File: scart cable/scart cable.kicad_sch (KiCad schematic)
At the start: 12 parts

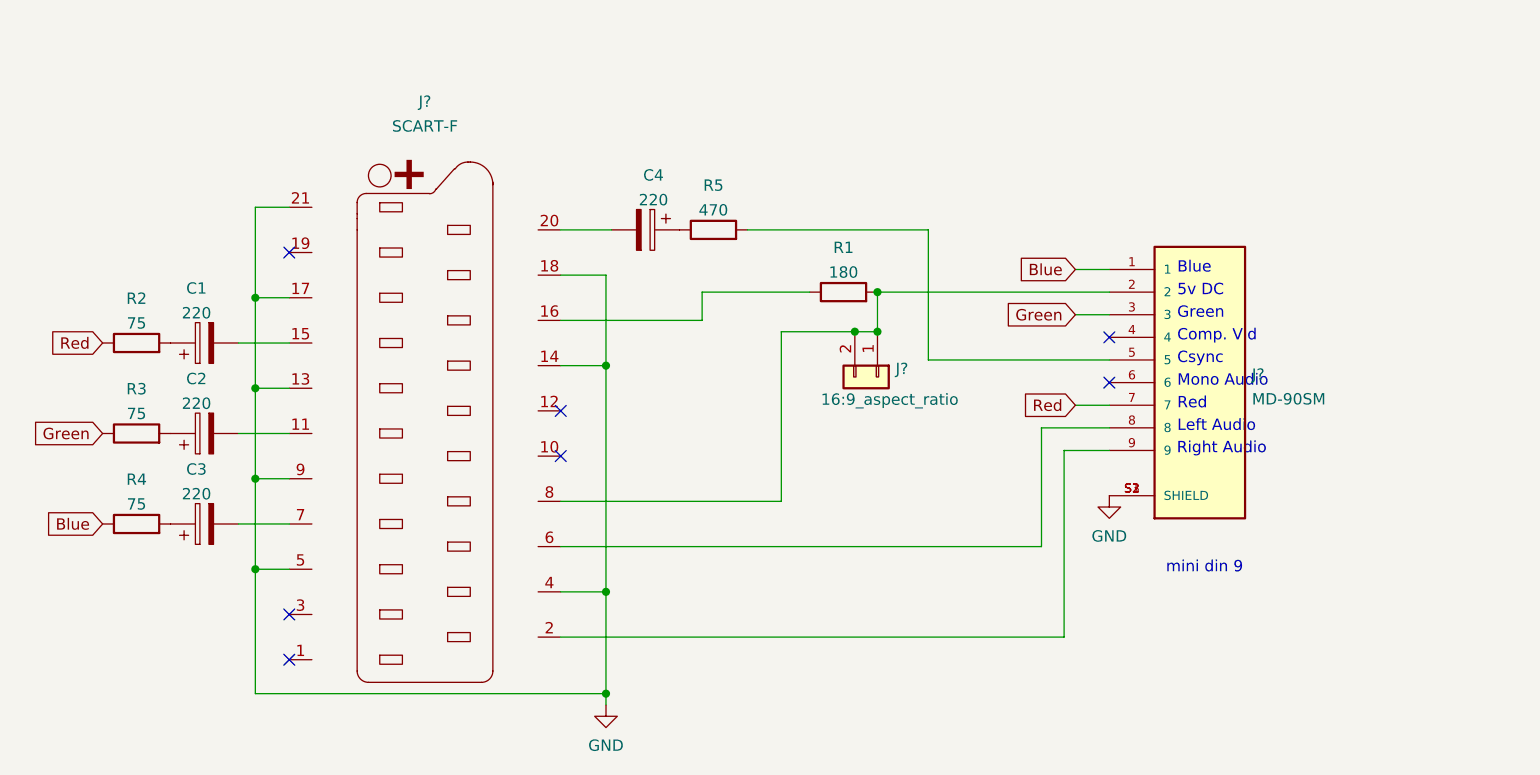
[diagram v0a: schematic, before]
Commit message: made scart cable board
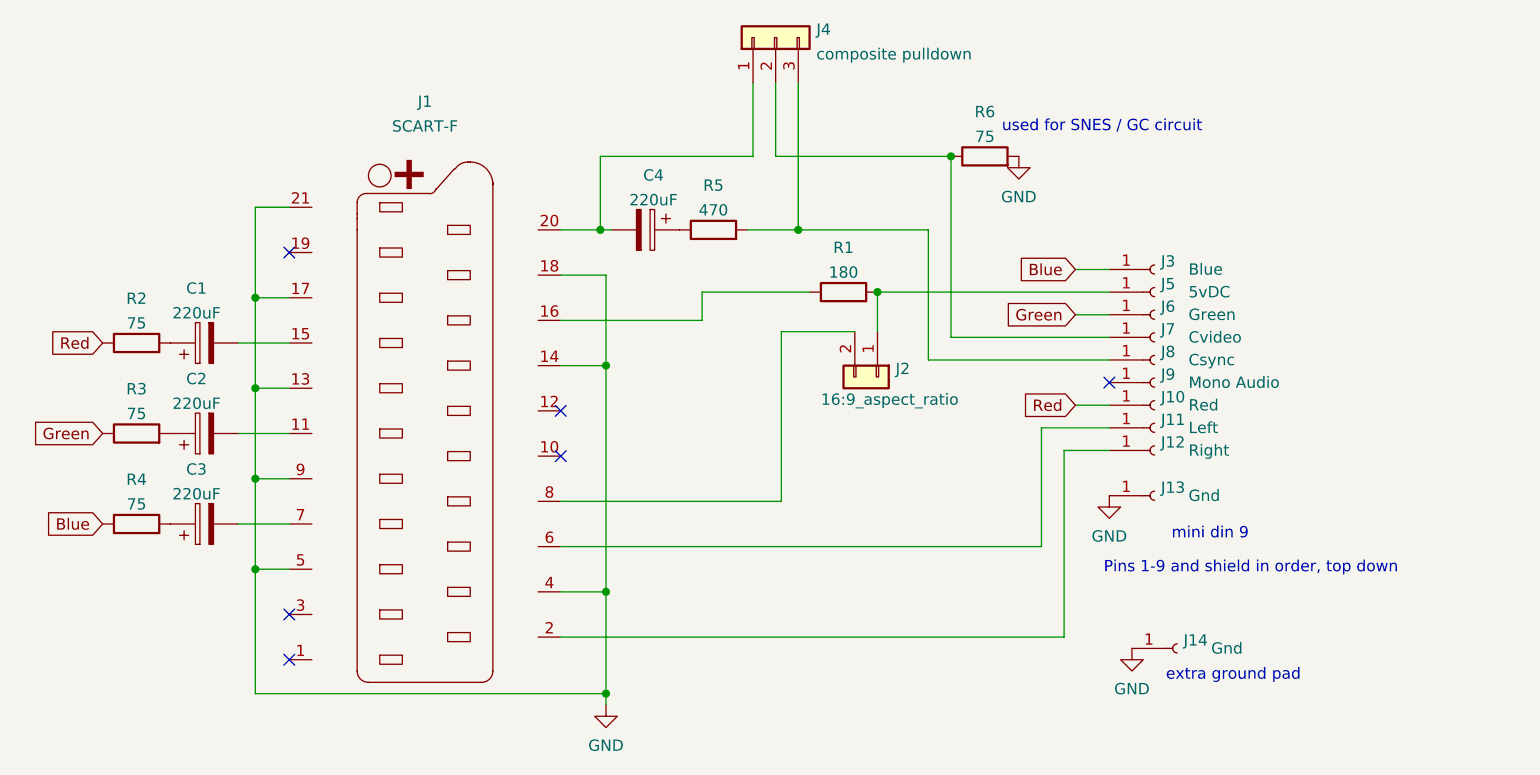
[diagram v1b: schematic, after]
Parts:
- removed J?: MD-90SM, CUI_MD-90SM, symbol Evan's misc parts:MD-90SM
- added J10: Red, Evan's misc parts:raw pad to splder to, symbol Connector:Conn_01x01_Female
- added J11: Left, Evan's misc parts:raw pad to splder to, symbol Connector:Conn_01x01_Female
- added J12: Right, Evan's misc parts:raw pad to splder to, symbol Connector:Conn_01x01_Female
- added J13, J14: Gnd, Evan's misc parts:raw pad to splder to, symbol Connector:Conn_01x01_Female
- added J3: Blue, Evan's misc parts:raw pad to splder to, symbol Connector:Conn_01x01_Female
- added J4: composite pulldown, Jumper:SolderJumper-3_P1.3mm_Open_RoundedPad1.0x1.5mm, symbol Connector_Generic:Conn_01x03
- added J5: 5vDC, Evan's misc parts:raw pad to splder to, symbol Connector:Conn_01x01_Female
- added J6: Green, Evan's misc parts:raw pad to splder to, symbol Connector:Conn_01x01_Female
- added J7: Cvideo, Evan's misc parts:raw pad to splder to, symbol Connector:Conn_01x01_Female
- added J8: Csync, Evan's misc parts:raw pad to splder to, symbol Connector:Conn_01x01_Female
- added J9: Mono Audio, Evan's misc parts:raw pad to splder to, symbol Connector:Conn_01x01_Female
- added R6: 75, Resistor_SMD:R_0603_1608Metric, symbol Device:R
- C1, C2, C3, C4: value 220 -> 220uF; footprint (none) -> Capacitor_SMD:CP_Elec_6.3x5.2
- J1: renamed from J?; footprint (none) -> Evan's misc parts:edge mount SCART
- J2: renamed from J?; footprint (none) -> Jumper:SolderJumper-2_P1.3mm_Bridged_RoundedPad1.0x1.5mm
- R1, R2, R3, R4, R5: footprint (none) -> Resistor_SMD:R_0603_1608Metric
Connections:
- net Blue: now also J3.1 (Pin_1)
- net GND: now also J13.1 (Pin_1), J14.1 (Pin_1), R6.2
- net Green: now also J6.1 (Pin_1)
- net Red: now also J10.1 (Pin_1)
- net at J2.1 (Pin_1), R1.2: now also J5.1 (Pin_1); no longer J1.8 (P8), J2.2 (Pin_2)
- net at R5.2: now also J4.3 (Pin_3), J8.1 (Pin_1)
- net at J1.6 (P6): now also J11.1 (Pin_1)
- net at J1.2 (P2): now also J12.1 (Pin_1)
- net at C4.2, J1.20 (P20): now also J4.1 (Pin_1)
- new net: J4.2 (Pin_2), J7.1 (Pin_1), R6.1
- new net: J1.8 (P8), J2.2 (Pin_2)
- no-connect marks 7 -> 6
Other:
- note added: "Pins 1-9 and shield in order, top down"
- note added: "extra ground pad"
- note added: "used for SNES / GC circuit"
- note removed: "5v DC"
- note removed: "Blue"
- note removed: "Comp. Vid"
- note removed: "Csync"
- note removed: "Green"
- note removed: "Left Audio"
- note removed: "Mono Audio"
- note removed: "Red"
- note removed: "Right Audio"
